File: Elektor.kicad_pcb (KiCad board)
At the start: 2 copper layers, 50 x 44 mm, 55 parts, among them J1 Conn_Coaxial, J13 Conn_Coaxial, J6 Conn_01x03_Pin, J8 Conn_01x02, Q1 BF545B, U1 Si5351A-B-GT, U2 74HC04, U3 74HC4066D_653, U5 MCP6022, U6 AUDIOSHIELD-REVD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

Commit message: alternative layout first commit
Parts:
- added C20: 100n, Capacitor_SMD:C_0603_1608Metric, F.Cu at (188.6, 94.0)
- moved RV1 28.3 mm to (165.0, 94.2)
- moved U2 17.1 mm to (182.4, 93.8)
- moved J6 10.9 mm to (164.0, 82.6)
- moved Y1 9.21 mm to (168.2, 85.4)
- moved U1 8.55 mm to (172.8, 86.0)
- moved C2 5.99 mm to (172.4, 90.6), turned to 0 degrees
- moved J8 5.58 mm to (169.8, 94.6)
- moved C16 1.00 mm to (176.5, 84.3)
- moved R2 0.86 mm to (175.4, 78.4), turned to 0 degrees
- moved R4 0.55 mm to (173.0, 78.2)
- moved R1 0.48 mm to (170.8, 78.2)
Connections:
- U2 pad 1: Net-(U1-CLK0) -> Net-(U2G-VCC)
- U2 pad 10: unconnected-(U2-Pad10) -> Net-(U3-4E)
- U2 pad 11: Net-(U2G-VCC) -> Net-(U1-CLK1)
- U2 pad 12: unconnected-(U2-Pad12) -> Net-(U3-1E)
- U2 pad 13: Net-(U2G-VCC) -> Net-(U1-CLK0)
- U2 pad 2: Net-(U3-1E) -> unconnected-(U2-Pad2)
- U2 pad 3: Net-(U1-CLK1) -> Net-(U2G-VCC)
- U2 pad 4: Net-(U3-4E) -> unconnected-(U2-Pad4)
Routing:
- net Net-(J13-In): track 12.9 -> 44.6 mm
- net Net-(U2G-VCC): track 41.0 -> 65.6 mm
- net GND: track 106.5 -> 83.4 mm, vias 6 -> 5
- net Net-(J6-Pin_3): track 30.1 -> 12.1 mm, vias 1 -> 0
- net Net-(U1-CLK0): track 33.6 -> 19.7 mm, vias 4 -> 2
- net Net-(U1-CLK1): track 31.9 -> 19.1 mm, vias 2 -> 0
- net Net-(U3-1E): track 19.5 -> 10.1 mm, vias 0 -> 2
- net Net-(U3-4E): track 18.7 -> 10.2 mm, vias 0 -> 2
- net 3.3V: track 86.1 -> 78.5 mm, vias 1 -> 3
- net Net-(U1-SDA): track 12.8 -> 5.24 mm
- net Net-(U1-SCL): track 14.3 -> 8.43 mm
- net Net-(J8-Pin_1): track 3.60 -> 7.73 mm
- net Net-(U3-2Z): track 16.3 -> 12.2 mm
- net Net-(U3-1Z): track 21.1 -> 18.3 mm
- net Net-(U3-1Y): track 15.7 -> 13.7 mm
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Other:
- board size 50 x 44 mm -> 50 x 40 mm

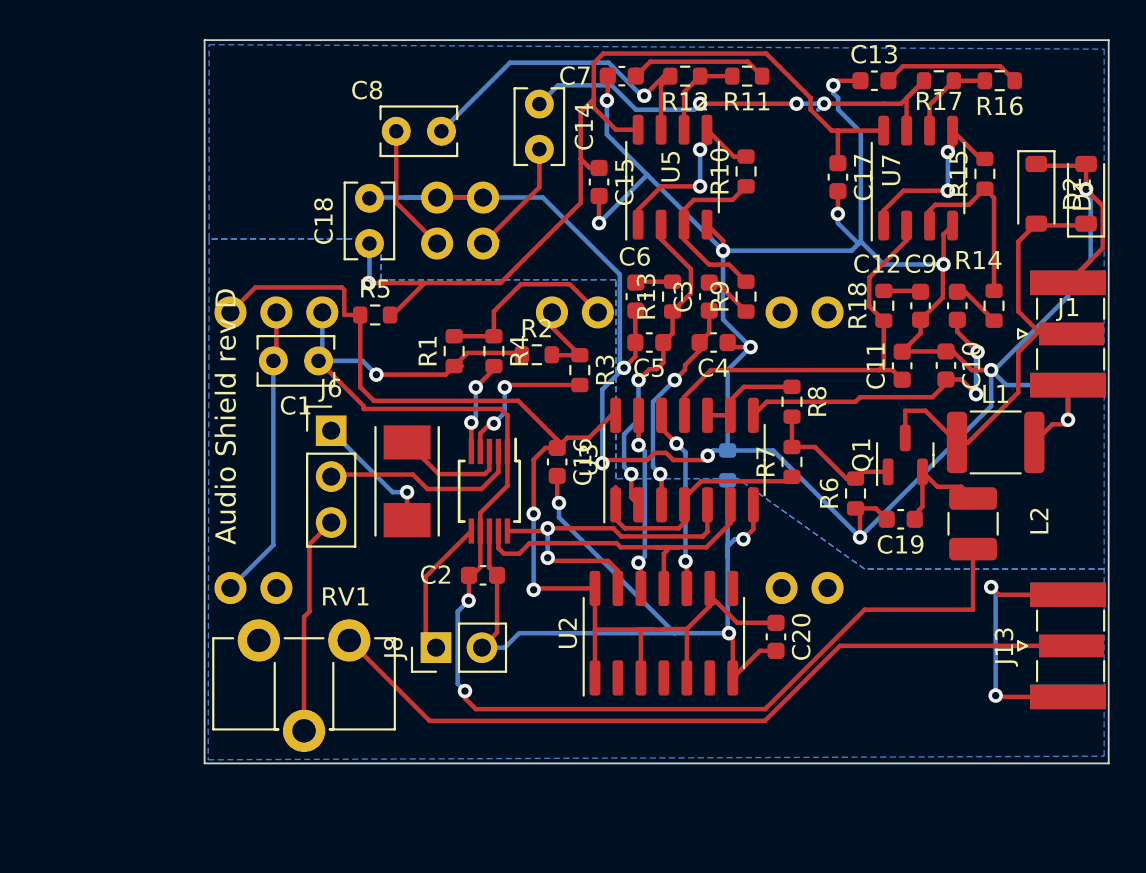
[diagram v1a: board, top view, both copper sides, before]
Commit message: pousse U1 a droite pour plus de compacite
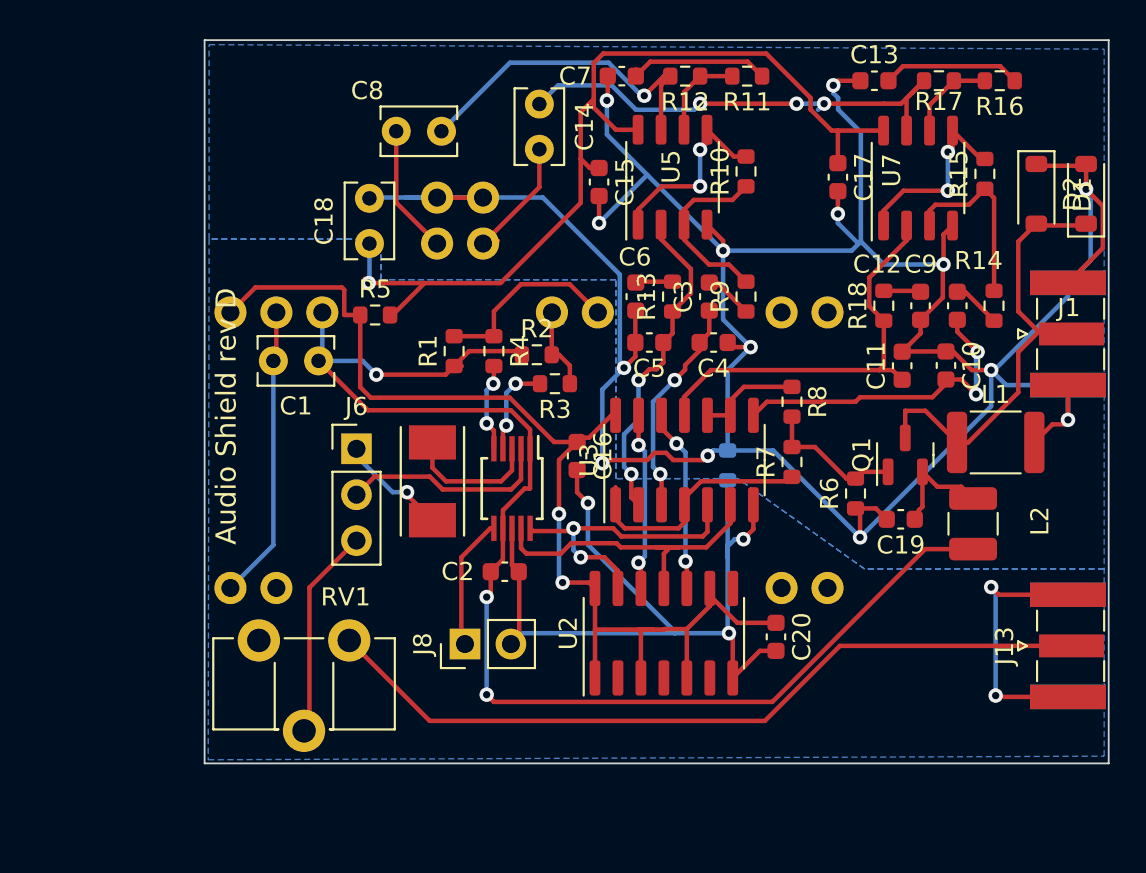
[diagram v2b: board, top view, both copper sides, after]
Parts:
- moved J6 1.72 mm to (165.4, 83.6)
- moved J8 1.61 mm to (171.4, 94.4)
- moved R3 1.57 mm to (176.4, 80.0), turned to 180 degrees
- moved Y1 1.40 mm to (169.6, 85.4)
- moved U1 1.26 mm to (174.0, 85.8)
- moved C2 1.22 mm to (173.6, 90.4)
- moved C16 1.15 mm to (177.6, 84.0)
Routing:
- net Net-(U1-SCL): track 8.43 -> 5.35 mm
- net Net-(U1-CLK0): track 19.7 -> 16.8 mm
- net 3.3V: track 78.5 -> 75.8 mm
- net Net-(U2G-VCC): track 65.6 -> 63.1 mm
- net GND: track 83.4 -> 81.4 mm
- net Net-(U1-XB): track 6.38 -> 7.56 mm
- net Net-(U1-CLK1): track 19.1 -> 18.0 mm
- net Net-(J6-Pin_1): track 7.16 -> 6.16 mm
- net Net-(U6-SCL): track 5.38 -> 6.26 mm
- net Net-(J6-Pin_2): track 11.2 -> 11.7 mm
